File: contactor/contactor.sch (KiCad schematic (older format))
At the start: 7 parts

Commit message: Starting Layout.
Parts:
- removed D? (x4): DIODE, symbol pspice:DIODE
- removed Q?: Q_NMOS_DGS, symbol Device:Q_NMOS_DGS
- removed R?: R, symbol Device:R
- added D1, D2, D3, D4: LED, LEDs:LED_1206, symbol Device:LED
- added D5: D, Diodes_SMD:D_1206, symbol Device:D
- added J1, J2, J3, J4, J5, J6, J7: Screw_Terminal_01x01, footprints:RingTerminal, symbol Connector:Screw_Terminal_01x01
- added Q1: Q_NMOS_DGS, TO_SOT_Packages_SMD:TO-263-3_TabPin2, symbol Device:Q_NMOS_DGS
- added R10, R11, R12, R13, R2, R3, R4, R5, R6, R7, R8, R9: 10k, Resistors_SMD:R_0805, symbol Device:R
- added U1: 74LS21, SMD_Packages:SOIC-14_N, symbol 74xx:74LS21
- R1: renamed from R?; value R -> 10k; footprint (none) -> Resistors_SMD:R_0805
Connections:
- net labels added: +12V, BMS_Fault_L, BMS_ISO_L, BMS_Spare_Fault_L, Contactor-, Inverter_Relay_L
- net labels removed: ISO, Inverter_Relay, Master_Fault, Slave_Fault
- wire segments 18 -> 57
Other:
- note added: "*This is the Contactor+ signal as well."
- moved on the sheet: R1

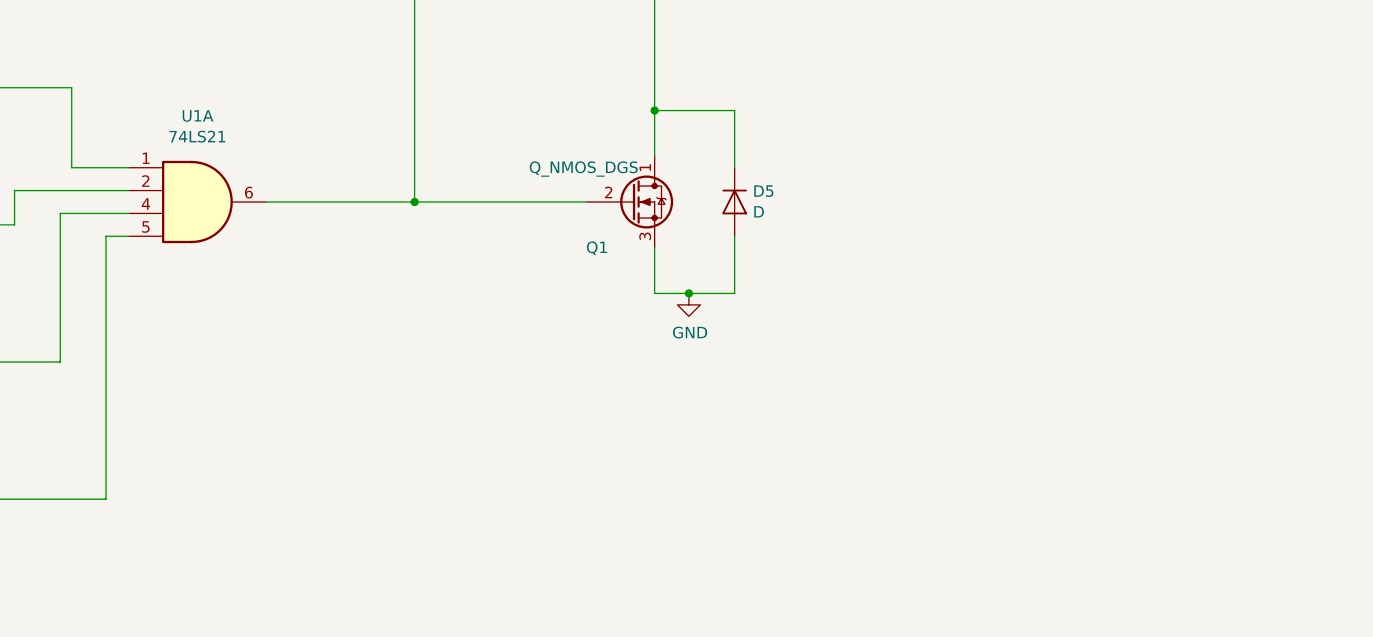
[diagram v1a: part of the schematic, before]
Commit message: Routing almost done, need to connect 12V traces
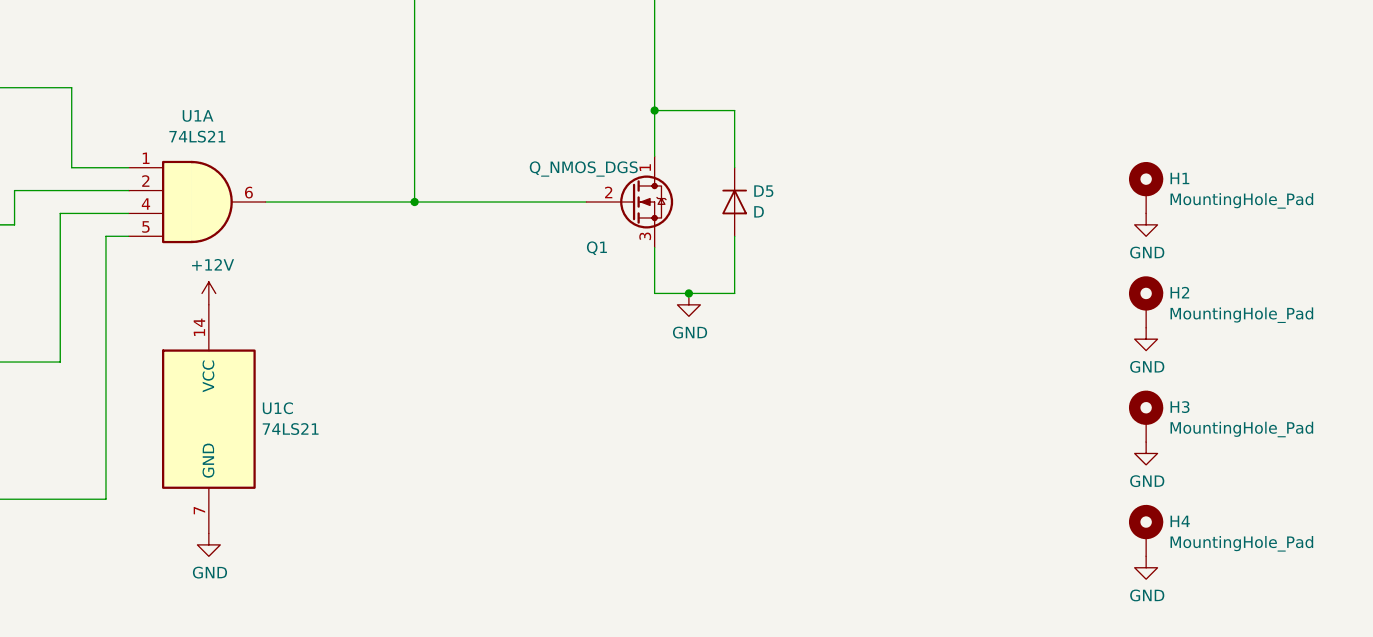
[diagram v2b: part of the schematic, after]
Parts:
- added H1, H2, H3, H4: MountingHole_Pad, Mounting_Holes:MountingHole_3.2mm_M3_Pad, symbol Mechanical:MountingHole_Pad
- added unit 3 of U1
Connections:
- net +12V: now also U1.14 (VCC)
- net GND: now also H1.1, H2.1, H3.1, H4.1, U1.7 (GND)
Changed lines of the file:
@@
+	1    0    0    -1
+$EndComp
+$Comp
+L Mechanical:MountingHole_Pad H2
+U 1 1 5CDC9CD1
+P 10300 5200
+F 0 "H2" H 10400 5251 50  0000 L CNN
+F 1 "MountingHole_Pad" H 10400 5160 50  0000 L CNN
+F 2 "Mounting_Holes:MountingHole_3.2mm_M3_Pad" H 10300 5200 50  0001 C CNN
+F 3 "~" H 10300 5200 50  0001 C CNN
+	1    10300 5200
+	1    0    0    -1
+$EndComp
+$Comp
+L power:GND #PWR0110
+U 1 1 5CDCCB43
+P 10300 5300
+F 0 "#PWR0110" H 10300 5050 50  0001 C CNN
+F 1 "GND" H 10305 5127 50  0000 C CNN
+F 2 "" H 10300 5300 50  0001 C CNN
+F 3 "" H 10300 5300 50  0001 C CNN
+	1    10300 5300
+	1    0    0    -1
+$EndComp
+$Comp
+L Mechanical:MountingHole_Pad H1
+U 1 1 5CDD3E6E
+P 10300 4700
+F 0 "H1" H 10400 4751 50  0000 L CNN
+F 1 "MountingHole_Pad" H 10400 4660 50  0000 L CNN
+F 2 "Mounting_Holes:MountingHole_3.2mm_M3_Pad" H 10300 4700 50  0001 C CNN
+F 3 "~" H 10300 4700 50  0001 C CNN
+	1    10300 4700
+	1    0    0    -1
+$EndComp
+$Comp
+L power:GND #PWR0111
+U 1 1 5CDD3E75
+P 10300 4800
+F 0 "#PWR0111" H 10300 4550 50  0001 C CNN
+F 1 "GND" H 10305 4627 50  0000 C CNN
+F 2 "" H 10300 4800 50  0001 C CNN
+F 3 "" H 10300 4800 50  0001 C CNN
+	1    10300 4800
+	1    0    0    -1
+$EndComp
+$Comp
+L Mechanical:MountingHole_Pad H4
+U 1 1 5CDD4E54
+P 10300 6200
+F 0 "H4" H 10400 6251 50  0000 L CNN
+F 1 "MountingHole_Pad" H 10400 6160 50  0000 L CNN
+F 2 "Mounting_Holes:MountingHole_3.2mm_M3_Pad" H 10300 6200 50  0001 C CNN
+F 3 "~" H 10300 6200 50  0001 C CNN
+	1    10300 6200
+	1    0    0    -1
+$EndComp
+$Comp
+L power:GND #PWR0112
+U 1 1 5CDD4E5B
+P 10300 6300
+F 0 "#PWR0112" H 10300 6050 50  0001 C CNN
+F 1 "GND" H 10305 6127 50  0000 C CNN
+F 2 "" H 10300 6300 50  0001 C CNN
+F 3 "" H 10300 6300 50  0001 C CNN
+	1    10300 6300
+	1    0    0    -1
+$EndComp
+$Comp
+L Mechanical:MountingHole_Pad H3
+U 1 1 5CDD4E61
+P 10300 5700
+F 0 "H3" H 10400 5751 50  0000 L CNN
+F 1 "MountingHole_Pad" H 10400 5660 50  0000 L CNN
+F 2 "Mounting_Holes:MountingHole_3.2mm_M3_Pad" H 10300 5700 50  0001 C CNN
+F 3 "~" H 10300 5700 50  0001 C CNN
+	1    10300 5700
+	1    0    0    -1
+$EndComp
+$Comp
+L power:GND #PWR0113
+U 1 1 5CDD4E68
+P 10300 5800
+F 0 "#PWR0113" H 10300 5550 50  0001 C CNN
+F 1 "GND" H 10305 5627 50  0000 C CNN
+F 2 "" H 10300 5800 50  0001 C CNN
+F 3 "" H 10300 5800 50  0001 C CNN
+	1    10300 5800
+	1    0    0    -1
+$EndComp
+$Comp
+L 74xx:74LS21 U1
+U 3 1 5CDD71C4
+P 6200 5700
+F 0 "U1" H 6430 5746 50  0000 L CNN
+F 1 "74LS21" H 6430 5655 50  0000 L CNN
+F 2 "" H 6200 5700 50  0001 C CNN
+F 3 "http://www.ti.com/lit/gpn/sn74LS21" H 6200 5700 50  0001 C CNN
+	3    6200 5700
+	1    0    0    -1
+$EndComp
+$Comp
+L power:+12V #PWR?
+U 1 1 5CDD7236
+P 6200 5200
+F 0 "#PWR?" H 6200 5050 50  0001 C CNN
+F 1 "+12V" H 6215 5373 50  0000 C CNN
+F 2 "" H 6200 5200 50  0001 C CNN
+F 3 "" H 6200 5200 50  0001 C CNN
+	1    6200 5200
+	1    0    0    -1
+$EndComp
+$Comp
+L power:GND #PWR?
+U 1 1 5CDD7281
+P 6200 6200
+F 0 "#PWR?" H 6200 5950 50  0001 C CNN
+F 1 "GND" H 6205 6027 50  0000 C CNN
+F 2 "" H 6200 6200 50  0001 C CNN
+F 3 "" H 6200 6200 50  0001 C CNN
+	1    6200 6200
 	1    0    0    -1
 $EndComp
